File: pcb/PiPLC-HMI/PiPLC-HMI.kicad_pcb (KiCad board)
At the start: 2 copper layers, 86.4 x 50 mm, 26 parts, among them J1 Conn_02x12_Odd_Even, J2 KNX

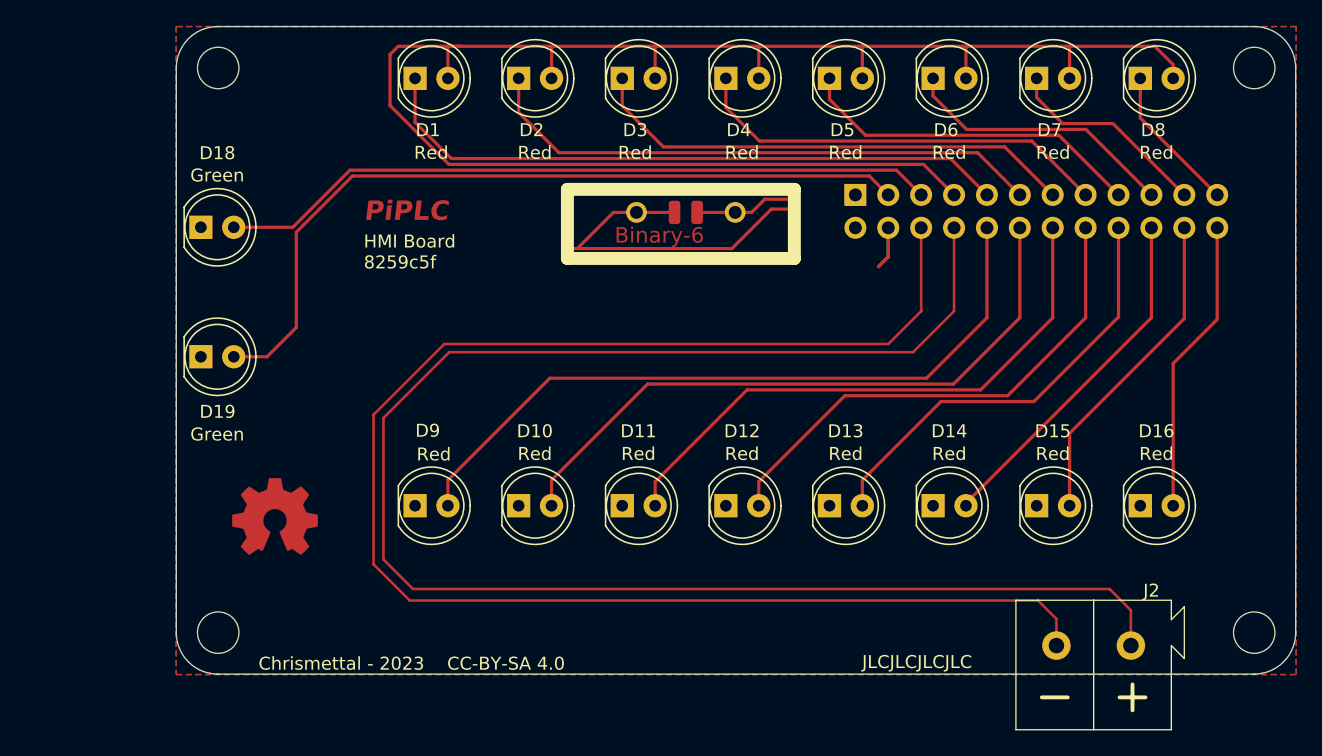
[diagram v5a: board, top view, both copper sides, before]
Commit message: [HMI] Fix Q LEDs inverted + add silk labels
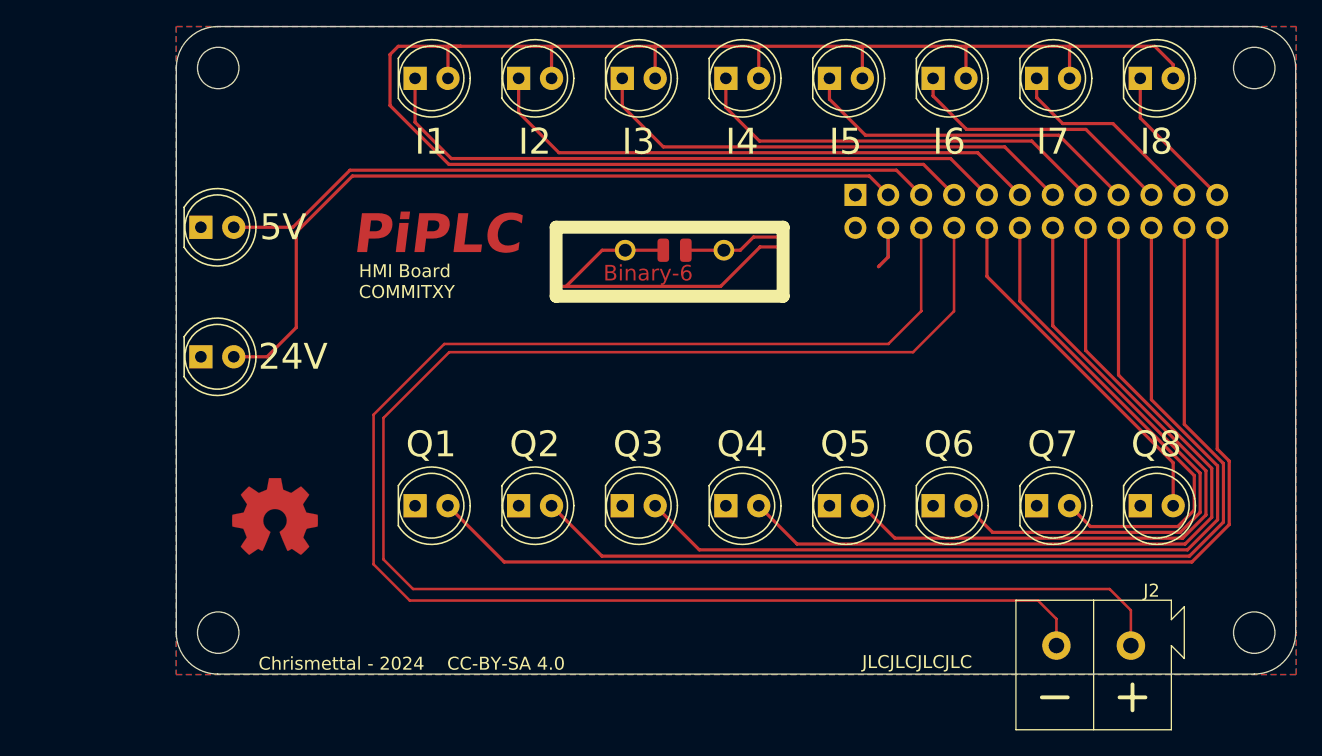
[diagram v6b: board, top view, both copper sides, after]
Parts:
- moved H7 3.05 mm to (168.0, 85.0)
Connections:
- D10 pad 2: /LED_Q7 -> /LED_Q2
- D11 pad 2: /LED_Q6 -> /LED_Q3
- D12 pad 2: /LED_Q5 -> /LED_Q4
- D13 pad 2: /LED_Q4 -> /LED_Q5
- D14 pad 2: /LED_Q3 -> /LED_Q6
- D15 pad 2: /LED_Q2 -> /LED_Q7
- D16 pad 2: /LED_Q1 -> /LED_Q8
- D9 pad 2: /LED_Q8 -> /LED_Q1
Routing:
- net /LED_Q1: track 22.9 -> 86.6 mm
- net /LED_Q2: track 25.1 -> 78.6 mm
- net /LED_Q3: track 27.4 -> 70.5 mm
- net /LED_Q4: track 33.9 -> 62.4 mm
- net /LED_Q8: track 55.7 -> 27.4 mm
- net /LED_Q5: track 39.3 -> 54.3 mm
- net /LED_Q7: track 50.3 -> 38.2 mm
- net /LED_Q6: track 44.7 -> 46.3 mm
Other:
- board text added: "24V"
- board text added: "5V"
- board text added: "Chrismettal - 2024 CC-BY-SA 4.0"
- board text added: "HMI Board COMMITXY"
- board text added: "I1"
- board text added: "I2"
- board text added: "I3"
- board text added: "I4"
- board text added: "I5"
- board text added: "I6"
- board text added: "I7"
- board text added: "I8"
- board text added: "Q1"
- board text added: "Q2"
- board text added: "Q3"
- board text added: "Q4"
- board text added: "Q5"
- board text added: "Q6"
- board text added: "Q7"
- board text added: "Q8"
- board text removed: "Chrismettal - 2023 CC-BY-SA 4.0"
- board text removed: "HMI Board 8259c5f"
